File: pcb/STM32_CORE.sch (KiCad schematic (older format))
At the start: 34 parts, among them J11 Conn_01x04, J12 Conn_01x04, J6 Conn_01x14, J7 Conn_01x12, J8 Conn_01x15, SW1 SW_Push, U3 STM32F103C8T6, U4 AMS1117-3.3, Y1 O8M, Y2 O_EPSON_32.768K

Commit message: update,
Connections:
- net labels added: STM32_PMS5003S_RX, STM32_PMS5003S_TX
- net labels removed: PMS5003S_RX, PMS5003S_TX
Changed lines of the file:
@@
 $Descr A3 16535 11693
 encoding utf-8
-Sheet 5 7
+Sheet 5 8
 Title ""
 Date ""
@@
 	11050 5350 11050 5550
 Text GLabel 10000 3150 2    50   Input ~ 0
-PMS5003S_RX
+STM32_PMS5003S_RX
 Text GLabel 10000 3250 2    50   Input ~ 0
-PMS5003S_TX
+STM32_PMS5003S_TX
 Text Label 6550 1400 2    50   ~ 0
 VBAT
@@
 	6100 1500 6100 1400
 $Comp
-L power:GND #PWR?
+L power:GND #PWR0116
 U 1 1 5BDB5D1B
 P 6100 2300
-F 0 "#PWR?" H 6100 2050 50  0001 C CNN
+F 0 "#PWR0116" H 6100 2050 50  0001 C CNN
 F 1 "GND" H 6105 2127 50  0000 C CNN
 F 2 "" H 6100 2300 50  0001 C CNN

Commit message: update,
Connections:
- net labels added: B2B_UART_RX, B2B_UART_TX, STM32_PMS7003S_RESET, STM32_PMS7003S_RXD, STM32_PMS7003S_SET, STM32_PMS7003S_TXD
- net labels removed: STM32_PMS5003S_RX, STM32_PMS5003S_TX
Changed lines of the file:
@@
 	11050 5350 11050 5550
 Text GLabel 10000 3150 2    50   Input ~ 0
-STM32_PMS5003S_RX
+STM32_PMS7003S_RXD
 Text GLabel 10000 3250 2    50   Input ~ 0
-STM32_PMS5003S_TX
+STM32_PMS7003S_TXD
 Text Label 6550 1400 2    50   ~ 0
 VBAT
@@
 Wire Wire Line
 	6100 2100 6100 2000
+Text GLabel 10000 2950 2    50   Input ~ 0
+STM32_PMS7003S_RESET
+Text GLabel 10000 3050 2    50   Input ~ 0
+STM32_PMS7003S_SET
+Text GLabel 8700 4750 3    50   Input ~ 0
+B2B_UART_TX
+Text GLabel 8800 4750 3    50   Input ~ 0
+B2B_UART_RX
 $EndSCHEMATC

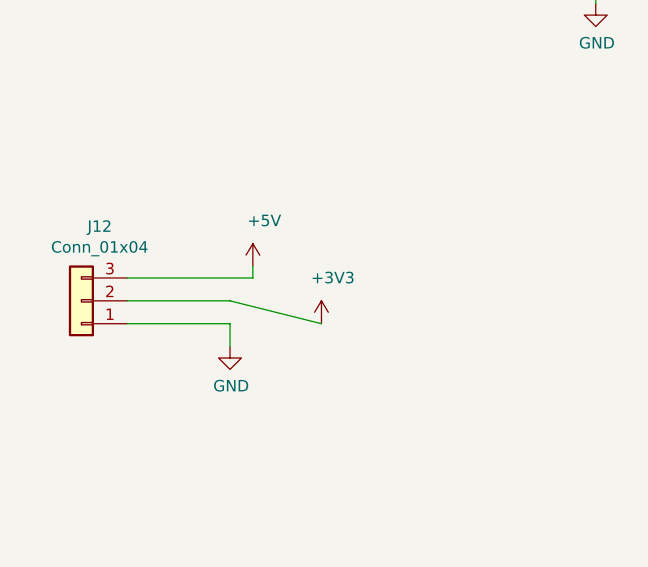
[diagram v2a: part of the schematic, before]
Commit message: update power source terminal,
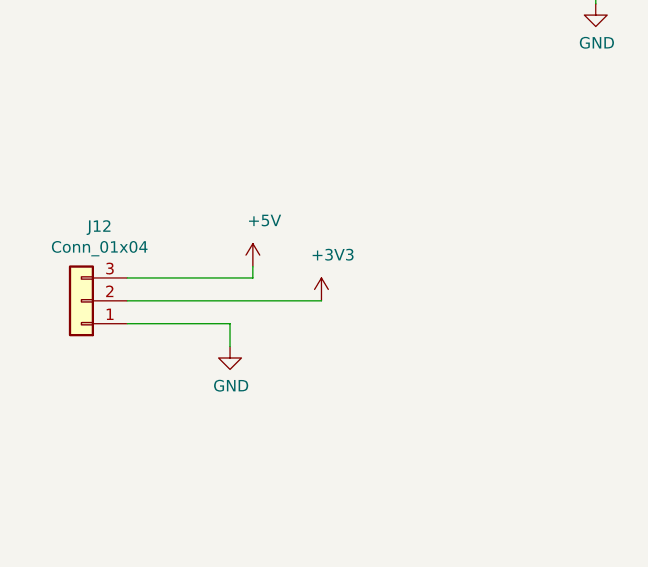
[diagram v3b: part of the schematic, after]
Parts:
- J12: footprint footprint-lib:Pin_Header_Straight_1x03_Pitch2.54mm -> w_conn_mkds:mkds_1,5-3
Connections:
- wire segments 191 -> 190
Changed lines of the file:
@@
 F 0 "J12" H 1520 5325 50  0000 C CNN
 F 1 "Conn_01x04" H 1520 5416 50  0000 C CNN
-F 2 "footprint-lib:Pin_Header_Straight_1x03_Pitch2.54mm" H 1600 5650 50  0001 C CNN
+F 2 "w_conn_mkds:mkds_1,5-3" H 1600 5650 50  0001 C CNN
 F 3 "~" H 1600 5650 50  0001 C CNN
 	1    1600 5650
@@
 Wire Wire Line
 	1800 5750 2250 5750
-Wire Wire Line
-	2650 5750 2250 5650
-Wire Wire Line
-	1800 5650 2250 5650
 $Comp
 L power:+3V3 #PWR0112
 U 1 1 5BD22354
-P 2650 5750
-F 0 "#PWR0112" H 2650 5600 50  0001 C CNN
-F 1 "+3V3" H 2700 5950 50  0000 C CNN
-F 2 "" H 2650 5750 50  0001 C CNN
-F 3 "" H 2650 5750 50  0001 C CNN
-	1    2650 5750
+P 2650 5650
+F 0 "#PWR0112" H 2650 5500 50  0001 C CNN
+F 1 "+3V3" H 2700 5850 50  0000 C CNN
+F 2 "" H 2650 5650 50  0001 C CNN
+F 3 "" H 2650 5650 50  0001 C CNN
+	1    2650 5650
 	1    0    0    -1
 $EndComp
@@
 Text GLabel 8800 4750 3    50   Input ~ 0
 B2B_UART_RX
+Wire Wire Line
+	1800 5650 2650 5650
 $EndSCHEMATC

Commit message: update adding SSR2 on pcb and ioc,
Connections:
- net labels added: STM32_SSR1_OUTPUT, STM32_SSR2_OUTPUT
- net labels removed: STM32_SSR_OUTPUT
- wire segments 190 -> 198
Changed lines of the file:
@@
 Text Label 8500 1650 3    50   ~ 0
 PB6
-Wire Wire Line
-	8500 1650 8500 2200
 Text Label 8400 1650 3    50   ~ 0
 PB7
-Wire Wire Line
-	8400 1650 8400 2200
 Text Label 8300 1650 3    50   ~ 0
 BOOT0
@@
 	0    -1   -1   0
 $EndComp
-Text GLabel 8400 1650 1    50   Input ~ 0
+Text GLabel 8150 1250 1    50   Input ~ 0
 I2C_SDA
-Text GLabel 8500 1650 1    50   Input ~ 0
+Text GLabel 8500 1250 1    50   Input ~ 0
 I2C_SCL
 Text GLabel 8600 1650 1    50   Input ~ 0
@@
 STM32_FAN_PWM_OUTPUT
 Text GLabel 8400 4750 3    50   Input ~ 0
-STM32_SSR_OUTPUT
+STM32_SSR1_OUTPUT
 Text GLabel 8500 4750 3    50   Input ~ 0
 STM32_SSR-25-DA_OUTPUT
@@
 Wire Wire Line
 	11050 5350 11050 5550
-Text GLabel 10000 3150 2    50   Input ~ 0
+Text GLabel 8800 4750 3    50   Input ~ 0
 STM32_PMS7003S_RXD
-Text GLabel 10000 3250 2    50   Input ~ 0
+Text GLabel 8700 4750 3    50   Input ~ 0
 STM32_PMS7003S_TXD
 Text Label 6550 1400 2    50   ~ 0
@@
 Text GLabel 10000 3050 2    50   Input ~ 0
 STM32_PMS7003S_SET
-Text GLabel 8700 4750 3    50   Input ~ 0
+Text GLabel 8350 1250 1    50   Input ~ 0
 B2B_UART_TX
-Text GLabel 8800 4750 3    50   Input ~ 0
+Text GLabel 8000 1250 1    50   Input ~ 0
 B2B_UART_RX
 Wire Wire Line
 	1800 5650 2650 5650
+Wire Wire Line
+	8350 1250 8350 1300
+Wire Wire Line
+	8350 1300 8500 1300
+Wire Wire Line
+	8500 1300 8500 1250
+Wire Wire Line
+	8500 1300 8500 2200
+Connection ~ 8500 1300
+Wire Wire Line
+	8000 1250 8000 1300
+Wire Wire Line
+	8000 1300 8150 1300
+Wire Wire Line
+	8150 1300 8150 1250
+Wire Wire Line
+	8150 1300 8150 1350
+Wire Wire Line
+	8150 1350 8400 1350
+Wire Wire Line
+	8400 1350 8400 2200
+Connection ~ 8150 1300
+Text GLabel 8300 4750 3    50   Input ~ 0
+STM32_SSR2_OUTPUT
 $EndSCHEMATC

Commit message: update,
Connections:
- net labels added: STM32_FAN_RPM
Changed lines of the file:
@@
 Text GLabel 8300 4750 3    50   Input ~ 0
 STM32_SSR2_OUTPUT
+Text GLabel 10000 3750 2    50   Input ~ 0
+STM32_FAN_RPM
 $EndSCHEMATC

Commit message: update,
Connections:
- wire segments 198 -> 199
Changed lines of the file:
@@
 L power:+3V3 #PWR0112
 U 1 1 5BD22354
-P 2650 5650
-F 0 "#PWR0112" H 2650 5500 50  0001 C CNN
-F 1 "+3V3" H 2700 5850 50  0000 C CNN
-F 2 "" H 2650 5650 50  0001 C CNN
-F 3 "" H 2650 5650 50  0001 C CNN
-	1    2650 5650
+P 2650 5600
+F 0 "#PWR0112" H 2650 5450 50  0001 C CNN
+F 1 "+3V3" H 2700 5800 50  0000 C CNN
+F 2 "" H 2650 5600 50  0001 C CNN
+F 3 "" H 2650 5600 50  0001 C CNN
+	1    2650 5600
 	1    0    0    -1
 $EndComp
@@
 Text GLabel 10000 3750 2    50   Input ~ 0
 STM32_FAN_RPM
+Wire Wire Line
+	2650 5600 2650 5650
 $EndSCHEMATC

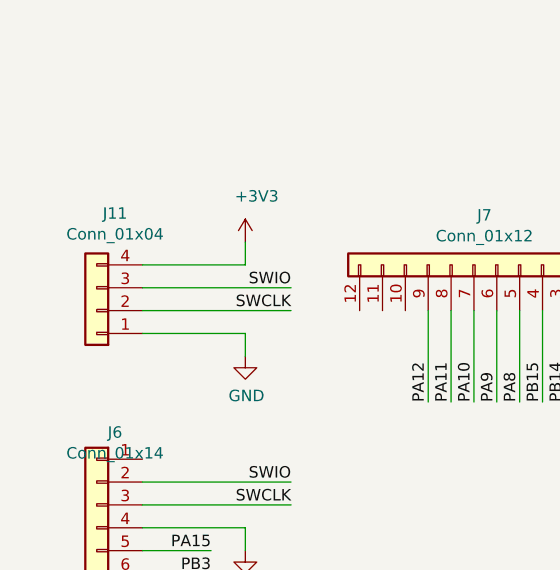
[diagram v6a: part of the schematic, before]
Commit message: update SWD_CONN pinout,
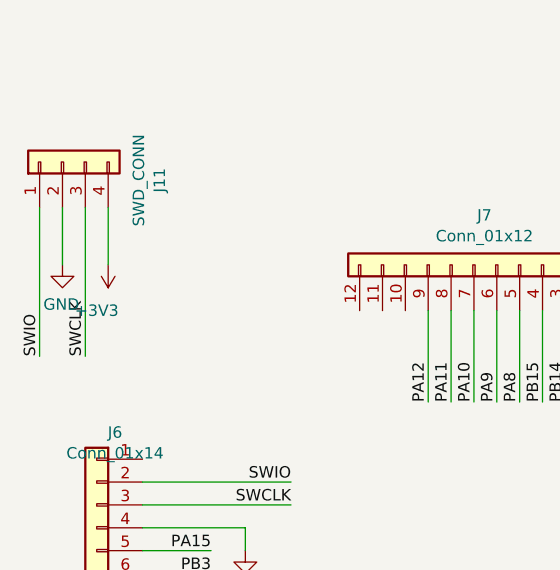
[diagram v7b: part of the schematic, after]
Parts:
- J11: value Conn_01x04 -> SWD_CONN
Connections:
- wire segments 199 -> 197
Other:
- moved on the sheet: J11
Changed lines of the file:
@@
 L Connector_Generic:Conn_01x04 J11
 U 1 1 5BD063FA
-P 1500 1850
-F 0 "J11" H 1420 1425 50  0000 C CNN
-F 1 "Conn_01x04" H 1420 1516 50  0000 C CNN
-F 2 "footprint-lib:Pin_Header_Straight_1x04_Pitch2.54mm" H 1500 1850 50  0001 C CNN
-F 3 "~" H 1500 1850 50  0001 C CNN
-	1    1500 1850
-	-1   0    0    1
-$EndComp
-Wire Wire Line
-	2150 1550 2150 1650
+P 1350 1200
+F 0 "J11" H 1270 775 50  0000 C CNN
+F 1 "SWD_CONN" H 1270 866 50  0000 C CNN
+F 2 "footprint-lib:Pin_Header_Straight_1x04_Pitch2.54mm" H 1350 1200 50  0001 C CNN
+F 3 "~" H 1350 1200 50  0001 C CNN
+	1    1350 1200
+	0    -1   -1   0
+$EndComp
 $Comp
 L power:GND #PWR0109
 U 1 1 5BD06547
-P 2150 2050
-F 0 "#PWR0109" H 2150 1800 50  0001 C CNN
-F 1 "GND" H 2155 1877 50  0000 C CNN
-F 2 "" H 2150 2050 50  0001 C CNN
-F 3 "" H 2150 2050 50  0001 C CNN
-	1    2150 2050
-	1    0    0    -1
-$EndComp
-Wire Wire Line
-	2150 1950 2150 2050
-Text Label 2350 1750 2    50   ~ 0
+P 1350 1650
+F 0 "#PWR0109" H 1350 1400 50  0001 C CNN
+F 1 "GND" H 1355 1477 50  0000 C CNN
+F 2 "" H 1350 1650 50  0001 C CNN
+F 3 "" H 1350 1650 50  0001 C CNN
+	1    1350 1650
+	-1   0    0    -1
+$EndComp
+Text Label 1250 2050 1    50   ~ 0
 SWIO
-Text Label 2350 1850 2    50   ~ 0
+Text Label 1450 2050 1    50   ~ 0
 SWCLK
 Wire Wire Line
-	1700 1950 2150 1950
-Wire Wire Line
-	1700 1850 2350 1850
-Wire Wire Line
-	1700 1750 2350 1750
-Wire Wire Line
-	1700 1650 2150 1650
+	1450 1400 1450 2050
+Wire Wire Line
+	1250 1400 1250 2050
 $Comp
 L power:+3V3 #PWR0110
 U 1 1 5BD06554
-P 2150 1550
-F 0 "#PWR0110" H 2150 1400 50  0001 C CNN
-F 1 "+3V3" H 2200 1750 50  0000 C CNN
-F 2 "" H 2150 1550 50  0001 C CNN
-F 3 "" H 2150 1550 50  0001 C CNN
-	1    2150 1550
-	1    0    0    -1
+P 1550 1650
+F 0 "#PWR0110" H 1550 1500 50  0001 C CNN
+F 1 "+3V3" H 1600 1850 50  0000 C CNN
+F 2 "" H 1550 1650 50  0001 C CNN
+F 3 "" H 1550 1650 50  0001 C CNN
+	1    1550 1650
+	-1   0    0    1
 $EndComp
 $Comp
@@
 Wire Wire Line
 	2650 5600 2650 5650
+Wire Wire Line
+	1550 1400 1550 1650
+Wire Wire Line
+	1350 1400 1350 1650
 $EndSCHEMATC

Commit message: update SWD_CONN pinout,
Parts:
- removed J11: SWD_CONN, footprint-lib:Pin_Header_Straight_1x04_Pitch2.54mm, symbol Connector_Generic:Conn_01x04
- added J?: SWD_CONN, symbol Connector_Generic:Conn_02x04_Odd_Even
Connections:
- net labels added: RST, SWIM
- wire segments 197 -> 201
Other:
- moved on the sheet: BOOT0, BOOT1, J6, JP1, R10, R9
